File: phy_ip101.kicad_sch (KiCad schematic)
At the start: 46 parts, among them U3 IP101GRI, X1 ASE-xxxMHz

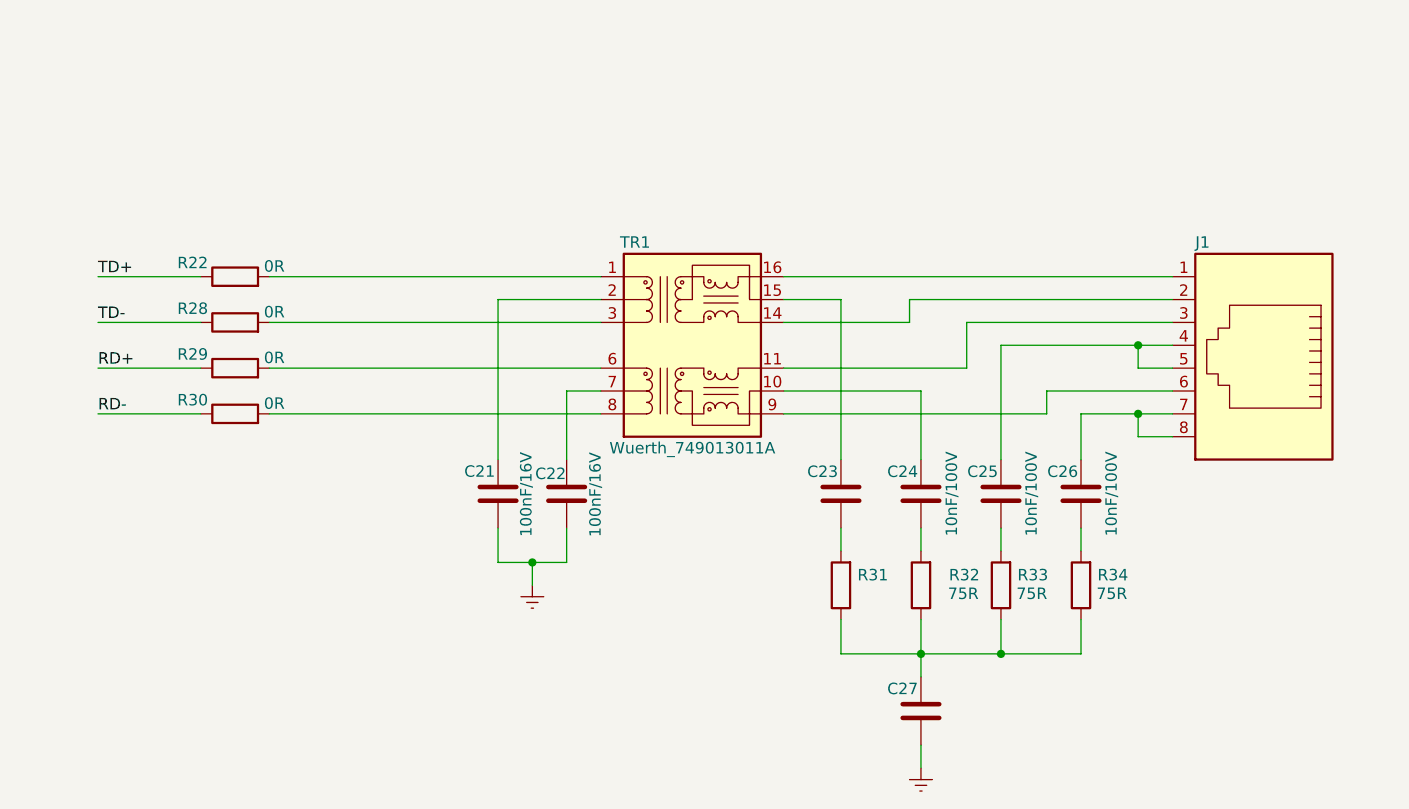
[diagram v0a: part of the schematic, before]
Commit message: Adicionado BG95-M3 e TVS do PHY Ethernet
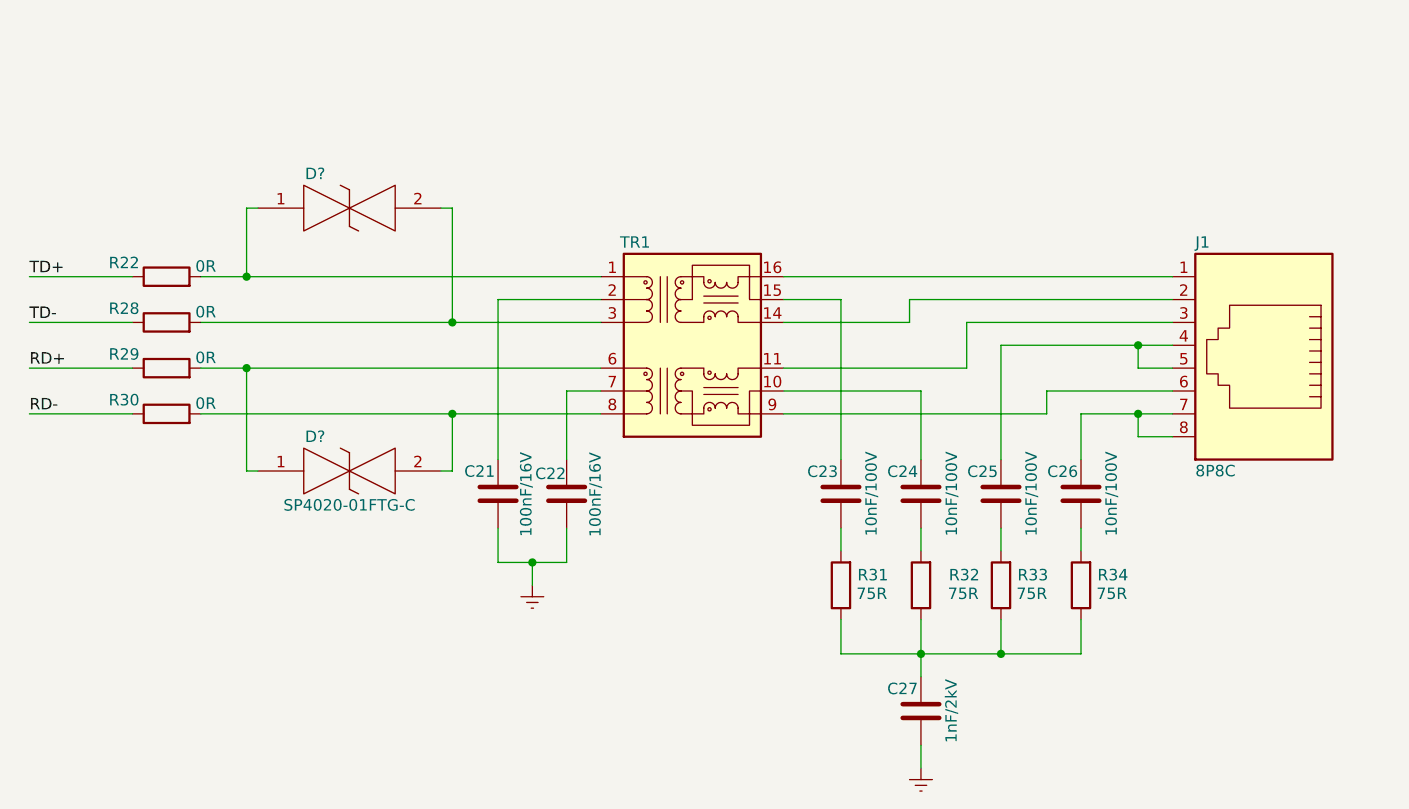
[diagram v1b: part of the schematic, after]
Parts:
- added D?: (no value), symbol Alexandre_Library:SP4020-01FTG-C
- added D?: SP4020-01FTG-C, Diode_SMD:D_SOD-323_HandSoldering, symbol Alexandre_Library:SP4020-01FTG-C
- C23: value (none) -> 10nF/100V
- C27: value (none) -> 1nF/2kV; footprint (none) -> Capacitor_SMD:C_1210_3225Metric_Pad1.33x2.70mm_HandSolder
- J1: value (none) -> 8P8C; footprint (none) -> Connector_RJ:RJ45_OST_PJ012-8P8CX_Vertical
- R31: value (none) -> 75R; footprint (none) -> Resistor_SMD:R_0402_1005Metric_Pad0.72x0.64mm_HandSolder
- TR1: value Wuerth_749013011A -> (none); footprint Transformer_SMD:Transformer_Ethernet_Wuerth_749013011A -> (none)
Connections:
- net at R22.2, TR1.1 (TD+): now also D?.1
- net at R28.2, TR1.3 (TD-): now also D?.2
- net at R29.2, TR1.6 (RD+): now also D?.1
- net at R30.2, TR1.8 (RD-): now also D?.2
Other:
- moved on the sheet: R22, R28, R29, R30

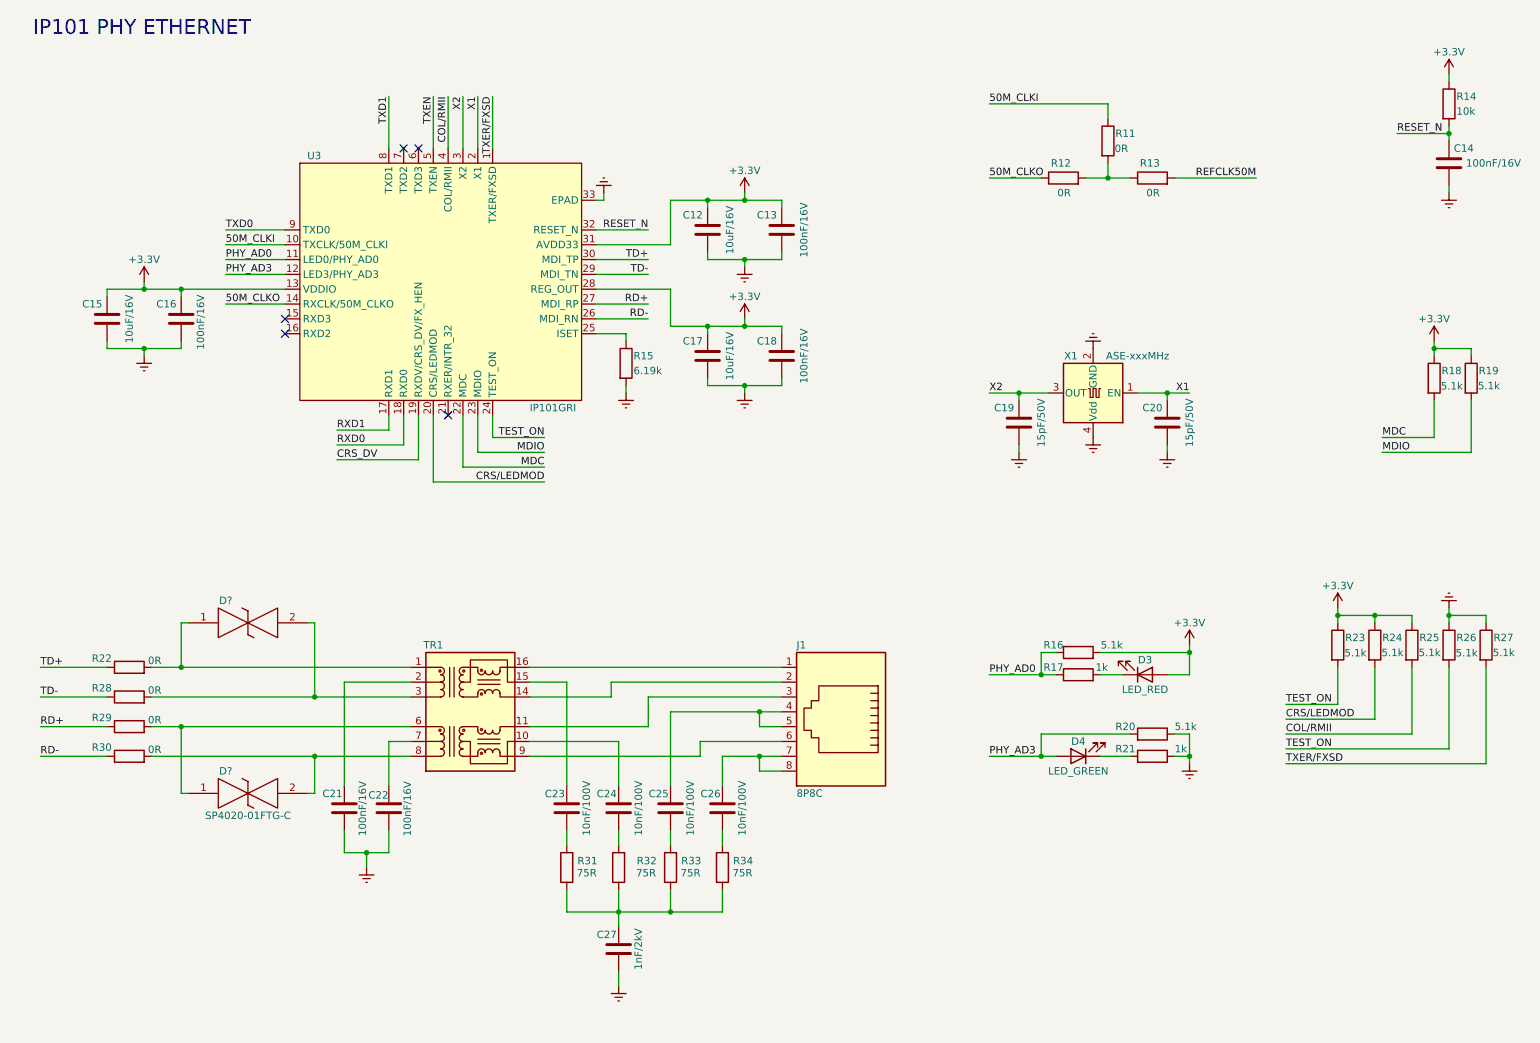
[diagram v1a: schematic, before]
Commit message: Adicionado o circuito de alimentação e reset do BG95
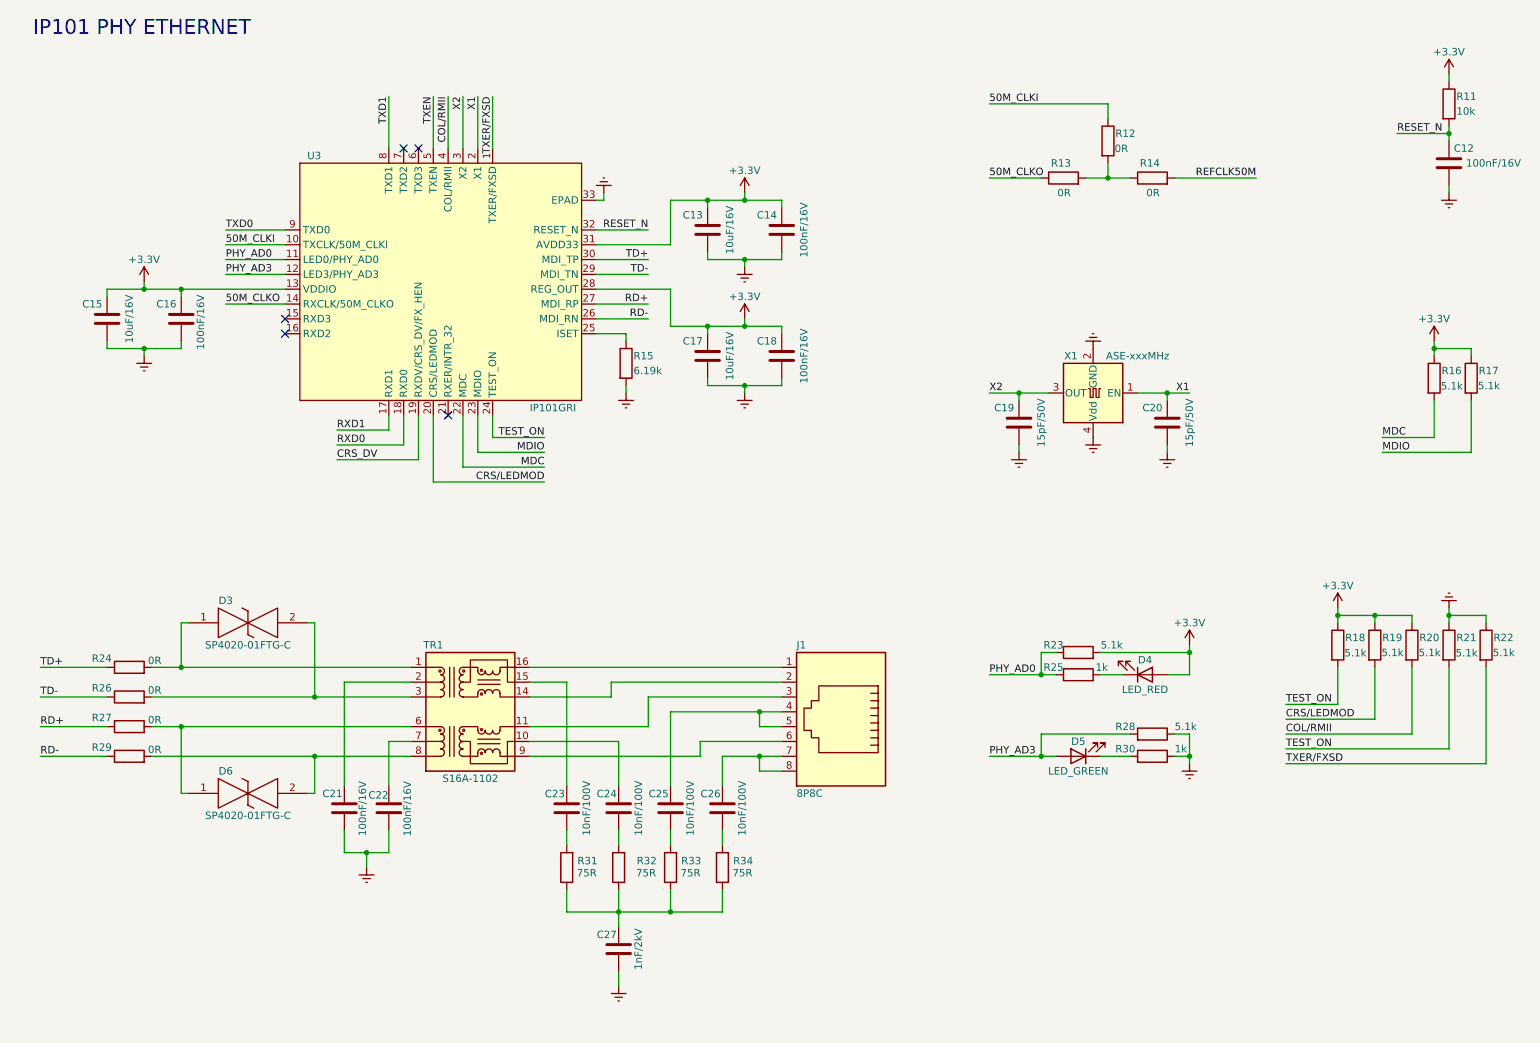
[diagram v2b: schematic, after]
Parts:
- D3: renamed from D?; value (none) -> SP4020-01FTG-C; footprint (none) -> Diode_SMD:D_SOD-323_HandSoldering
- TR1: value (none) -> S16A-1102; footprint (none) -> Transformer_SMD:Transformer_Ethernet_Wuerth_749013011A
- gave numbers to parts that had none: 1
- renumbered C14 to C12, C12 to C13, C13 to C14, D3 to D4, D4 to D5, R14 to R11, R11 to R12, R12 to R13, R13 to R14, R18 to R16, R19 to R17, R23 to R18, R24 to R19, R25 to R20, R26 to R21, R27 to R22, R16 to R23, R22 to R24, R17 to R25, R28 to R26, R29 to R27, R20 to R28, R30 to R29, R21 to R30

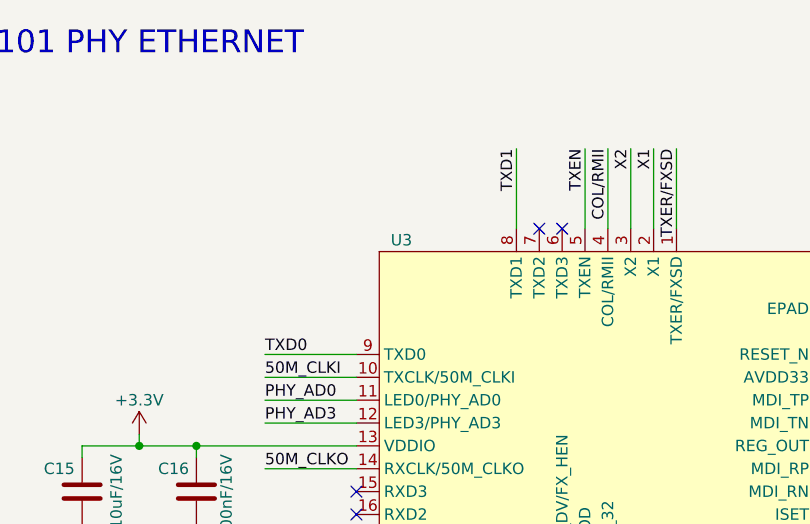
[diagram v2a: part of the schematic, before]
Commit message: Adicionado regulador 3.3V
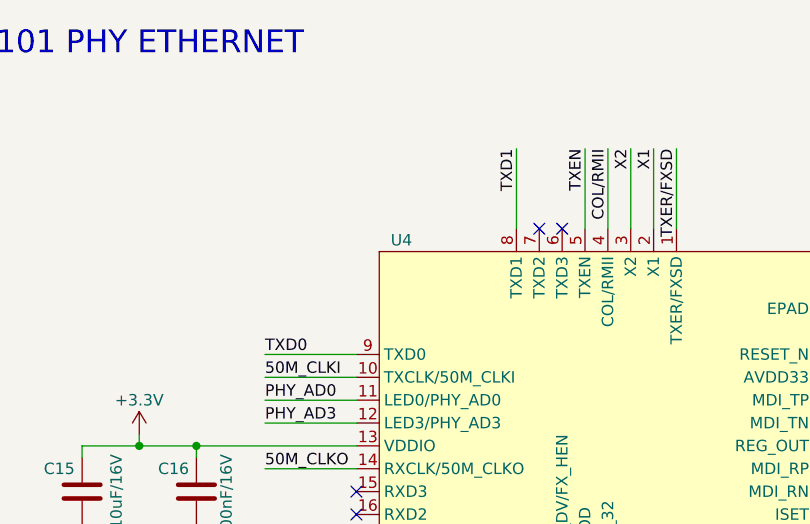
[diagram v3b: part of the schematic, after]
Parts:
- renumbered U3 to U4
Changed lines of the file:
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@@
   (symbol (lib_id "power:GNDREF") (at 116.84 50.8 180) (unit 1)
     (in_bom yes) (on_board yes) (fields_autoplaced)
-    (property "Reference" "#PWR033" (id 0) (at 116.84 44.45 0)
+    (property "Reference" "#PWR035" (id 0) (at 116.84 44.45 0)
       (effects (font (size 1.27 1.27)) hide)
     )
@@
   (symbol (lib_id "power:GNDREF") (at 187.96 95.25 0) (unit 1)
     (in_bom yes) (on_board yes) (fields_autoplaced)
-    (property "Reference" "#PWR045" (id 0) (at 187.96 101.6 0)
+    (property "Reference" "#PWR047" (id 0) (at 187.96 101.6 0)
       (effects (font (size 1.27 1.27)) hide)
     )
@@
   (symbol (lib_id "power:+3.3V") (at 140.97 50.8 0) (unit 1)
     (in_bom yes) (on_board yes)
-    (property "Reference" "#PWR034" (id 0) (at 140.97 54.61 0)
+    (property "Reference" "#PWR036" (id 0) (at 140.97 54.61 0)
       (effects (font (size 1.27 1.27)) hide)
     )
@@
   (symbol (lib_id "power:+3.3V") (at 242.57 121.92 0) (unit 1)
     (in_bom yes) (on_board yes)
-    (property "Reference" "#PWR047" (id 0) (at 242.57 125.73 0)
+    (property "Reference" "#PWR049" (id 0) (at 242.57 125.73 0)
       (effects (font (size 1.27 1.27)) hide)
     )
@@
   (symbol (lib_id "power:GNDREF") (at 140.97 63.5 0) (unit 1)
     (in_bom yes) (on_board yes) (fields_autoplaced)
-    (property "Reference" "#PWR036" (id 0) (at 140.97 69.85 0)
+    (property "Reference" "#PWR038" (id 0) (at 140.97 69.85 0)
       (effects (font (size 1.27 1.27)) hide)
     )
@@
   (symbol (lib_id "power:GNDREF") (at 76.2 166.37 0) (unit 1)
     (in_bom yes) (on_board yes) (fields_autoplaced)
-    (property "Reference" "#PWR051" (id 0) (at 76.2 172.72 0)
+    (property "Reference" "#PWR053" (id 0) (at 76.2 172.72 0)
       (effects (font (size 1.27 1.27)) hide)
     )
@@
   (symbol (lib_id "power:GNDREF") (at 38.1 78.74 0) (unit 1)
     (in_bom yes) (on_board yes) (fields_autoplaced)
-    (property "Reference" "#PWR041" (id 0) (at 38.1 85.09 0)
+    (property "Reference" "#PWR043" (id 0) (at 38.1 85.09 0)
       (effects (font (size 1.27 1.27)) hide)
     )
@@
   (symbol (lib_id "power:GNDREF") (at 217.17 148.59 0) (unit 1)
     (in_bom yes) (on_board yes) (fields_autoplaced)
-    (property "Reference" "#PWR050" (id 0) (at 217.17 154.94 0)
+    (property "Reference" "#PWR052" (id 0) (at 217.17 154.94 0)
       (effects (font (size 1.27 1.27)) hide)
     )
@@
   (symbol (lib_id "power:GNDREF") (at 261.62 121.92 180) (unit 1)
     (in_bom yes) (on_board yes) (fields_autoplaced)
-    (property "Reference" "#PWR048" (id 0) (at 261.62 115.57 0)
+    (property "Reference" "#PWR050" (id 0) (at 261.62 115.57 0)
       (effects (font (size 1.27 1.27)) hide)
     )
@@
   (symbol (lib_id "power:GNDREF") (at 261.62 50.8 0) (unit 1)
     (in_bom yes) (on_board yes) (fields_autoplaced)
-    (property "Reference" "#PWR035" (id 0) (at 261.62 57.15 0)
+    (property "Reference" "#PWR037" (id 0) (at 261.62 57.15 0)
       (effects (font (size 1.27 1.27)) hide)
     )
@@
   (symbol (lib_id "power:+3.3V") (at 217.17 128.27 0) (unit 1)
     (in_bom yes) (on_board yes)
-    (property "Reference" "#PWR049" (id 0) (at 217.17 132.08 0)
+    (property "Reference" "#PWR051" (id 0) (at 217.17 132.08 0)
       (effects (font (size 1.27 1.27)) hide)
     )
@@
   (symbol (lib_id "power:GNDREF") (at 119.38 186.69 0) (unit 1)
     (in_bom yes) (on_board yes) (fields_autoplaced)
-    (property "Reference" "#PWR052" (id 0) (at 119.38 193.04 0)
+    (property "Reference" "#PWR054" (id 0) (at 119.38 193.04 0)
       (effects (font (size 1.27 1.27)) hide)
     )
@@
   (symbol (lib_id "power:GNDREF") (at 200.66 77.47 180) (unit 1)
     (in_bom yes) (on_board yes) (fields_autoplaced)
-    (property "Reference" "#PWR040" (id 0) (at 200.66 71.12 0)
+    (property "Reference" "#PWR042" (id 0) (at 200.66 71.12 0)
       (effects (font (size 1.27 1.27)) hide)
     )
@@
   (symbol (lib_id "power:+3.3V") (at 259.08 76.2 0) (unit 1)
     (in_bom yes) (on_board yes)
-    (property "Reference" "#PWR039" (id 0) (at 259.08 80.01 0)
+    (property "Reference" "#PWR041" (id 0) (at 259.08 80.01 0)
       (effects (font (size 1.27 1.27)) hide)
     )
@@
   (symbol (lib_id "power:GNDREF") (at 120.65 85.09 0) (unit 1)
     (in_bom yes) (on_board yes) (fields_autoplaced)
-    (property "Reference" "#PWR042" (id 0) (at 120.65 91.44 0)
+    (property "Reference" "#PWR044" (id 0) (at 120.65 91.44 0)
       (effects (font (size 1.27 1.27)) hide)
     )
@@
   (symbol (lib_id "power:+3.3V") (at 140.97 72.39 0) (unit 1)
     (in_bom yes) (on_board yes)
-    (property "Reference" "#PWR038" (id 0) (at 140.97 76.2 0)
+    (property "Reference" "#PWR040" (id 0) (at 140.97 76.2 0)
       (effects (font (size 1.27 1.27)) hide)
     )
@@
   (symbol (lib_id "power:+3.3V") (at 38.1 66.04 0) (unit 1)
     (in_bom yes) (on_board yes)
-    (property "Reference" "#PWR037" (id 0) (at 38.1 69.85 0)
+    (property "Reference" "#PWR039" (id 0) (at 38.1 69.85 0)
       (effects (font (size 1.27 1.27)) hide)
     )
@@
   (symbol (lib_id "power:+3.3V") (at 261.62 30.48 0) (unit 1)
     (in_bom yes) (on_board yes)
-    (property "Reference" "#PWR032" (id 0) (at 261.62 34.29 0)
+    (property "Reference" "#PWR034" (id 0) (at 261.62 34.29 0)
       (effects (font (size 1.27 1.27)) hide)
     )
@@
   (symbol (lib_id "power:GNDREF") (at 140.97 85.09 0) (unit 1)
     (in_bom yes) (on_board yes) (fields_autoplaced)
-    (property "Reference" "#PWR043" (id 0) (at 140.97 91.44 0)
+    (property "Reference" "#PWR045" (id 0) (at 140.97 91.44 0)
       (effects (font (size 1.27 1.27)) hide)
     )
@@
   (symbol (lib_id "power:GNDREF") (at 213.36 95.25 0) (unit 1)
     (in_bom yes) (on_board yes) (fields_autoplaced)
-    (property "Reference" "#PWR046" (id 0) (at 213.36 101.6 0)
+    (property "Reference" "#PWR048" (id 0) (at 213.36 101.6 0)
       (effects (font (size 1.27 1.27)) hide)
     )
@@
   (symbol (lib_id "Alexandre_Library:IP101GR") (at 64.77 45.72 0) (unit 1)
     (in_bom yes) (on_board yes)
-    (property "Reference" "U3" (id 0) (at 66.04 44.45 0)
+    (property "Reference" "U4" (id 0) (at 66.04 44.45 0)
       (effects (font (size 1.27 1.27)) (justify left))
     )
@@
   (symbol (lib_id "power:GNDREF") (at 200.66 92.71 0) (unit 1)
     (in_bom yes) (on_board yes) (fields_autoplaced)
-    (property "Reference" "#PWR044" (id 0) (at 200.66 99.06 0)
-      (effects (font (size 1.27 1.27)) hide)
-    )
+    (property "Reference" "#PWR046" (id 0) (at 200.66 99.06 0)
+      (effects (font (size 1.27 1.27)) hide)
+    )
